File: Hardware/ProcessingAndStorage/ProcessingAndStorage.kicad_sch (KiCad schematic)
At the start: 0 parts

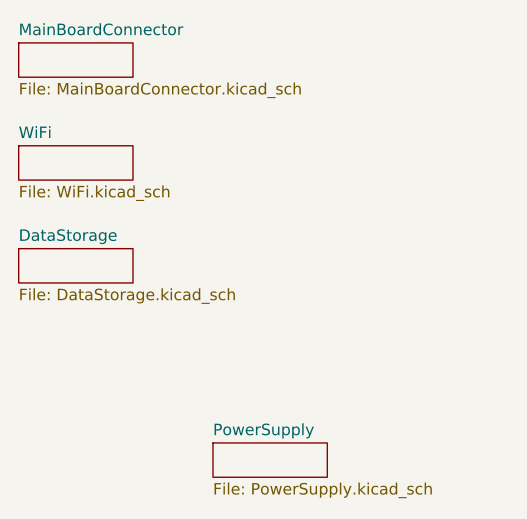
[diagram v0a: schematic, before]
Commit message: rework CI, make PCB smaller
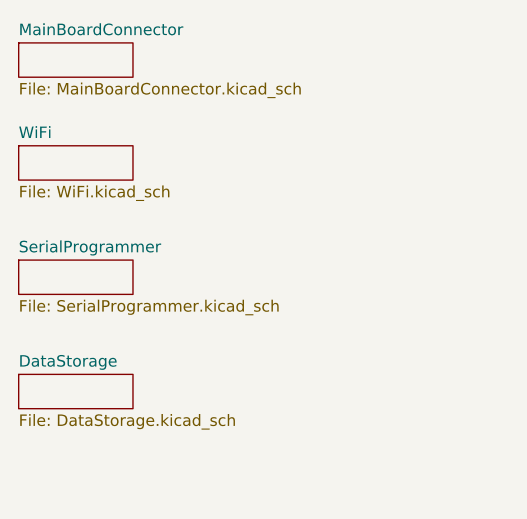
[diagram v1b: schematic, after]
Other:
- removed sheet PowerSupply
- added sheet SerialProgrammer (SerialProgrammer.kicad_sch)
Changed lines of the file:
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@@
 	(paper "A4")
+	(sheet
+		(at 53.34 87.63)
+		(size 12.7 3.81)
+		(exclude_from_sim no)
+		(in_bom yes)
+		(on_board yes)
+		(dnp no)
+		(fields_autoplaced yes)
+		(stroke
+			(width 0.1524)
+			(type solid)
+		)
+		(fill
+			(color 0 0 0 0.0000)
+		)
+		(property "Sheetname" "SerialProgrammer"
+			(at 53.34 86.9184 0)
+			(effects
+				(font
+					(size 1.27 1.27)
+				)
+				(justify left bottom)
+			)
+		)
+		(property "Sheetfile" "SerialProgrammer.kicad_sch"
+			(at 53.34 92.0246 0)
+			(effects
+				(font
+					(size 1.27 1.27)
+				)
+				(justify left top)
+			)
+		)
+		(instances
+			(project "ProcessingAndStorage"
+				(path "/2dac91f6-5de1-492e-9a04-36ab71ef854f"
+					(page "6")
+				)
+			)
+		)
+	)
 	(sheet
 		(at 53.34 74.93)
@@
 	)
 	(sheet
-		(at 74.93 107.95)
-		(size 12.7 3.81)
-		(exclude_from_sim no)
-		(in_bom yes)
-		(on_board yes)
-		(dnp no)
-		(fields_autoplaced yes)
-		(stroke
-			(width 0.1524)
-			(type solid)
-		)
-		(fill
-			(color 0 0 0 0.0000)
-		)
-		(property "Sheetname" "PowerSupply"
-			(at 74.93 107.2384 0)
-			(effects
-				(font
-					(size 1.27 1.27)
-				)
-				(justify left bottom)
-			)
-		)
-		(property "Sheetfile" "PowerSupply.kicad_sch"
-			(at 74.93 112.3446 0)
-			(effects
-				(font
-					(size 1.27 1.27)
-				)
-				(justify left top)
-			)
-		)
-		(instances
-			(project "ProcessingAndStorage"
-				(path "/2dac91f6-5de1-492e-9a04-36ab71ef854f"
-					(page "5")
-				)
-			)
-		)
-	)
-	(sheet
-		(at 53.34 86.36)
+		(at 53.34 100.33)
 		(size 12.7 3.81)
 		(exclude_from_sim no)
@@
 		)
 		(property "Sheetname" "DataStorage"
-			(at 53.34 85.6484 0)
+			(at 53.34 99.6184 0)
 			(effects
 				(font
@@
 		)
 		(property "Sheetfile" "DataStorage.kicad_sch"
-			(at 53.34 90.7546 0)
+			(at 53.34 104.7246 0)
 			(effects
 				(font
